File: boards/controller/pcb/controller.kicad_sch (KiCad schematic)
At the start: 5 parts, among them J101 Battery, J102 Load Switch 5V, J103 Load Switch 15 V isolated

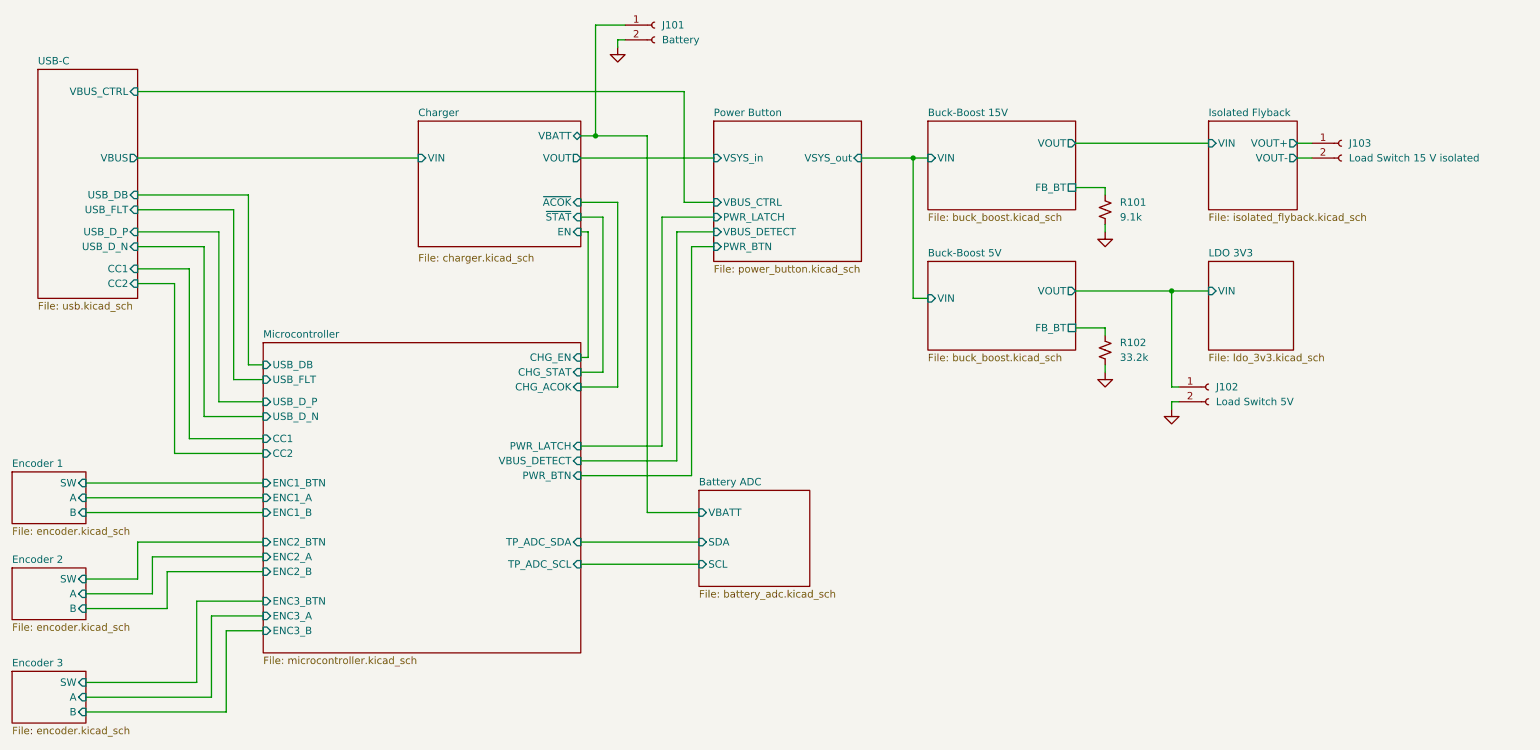
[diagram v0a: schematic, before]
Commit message: controller: pcb: Update schematic
Signed-off-by: Nicholas Loehrke <nicholasnloehrke@gmail.com>
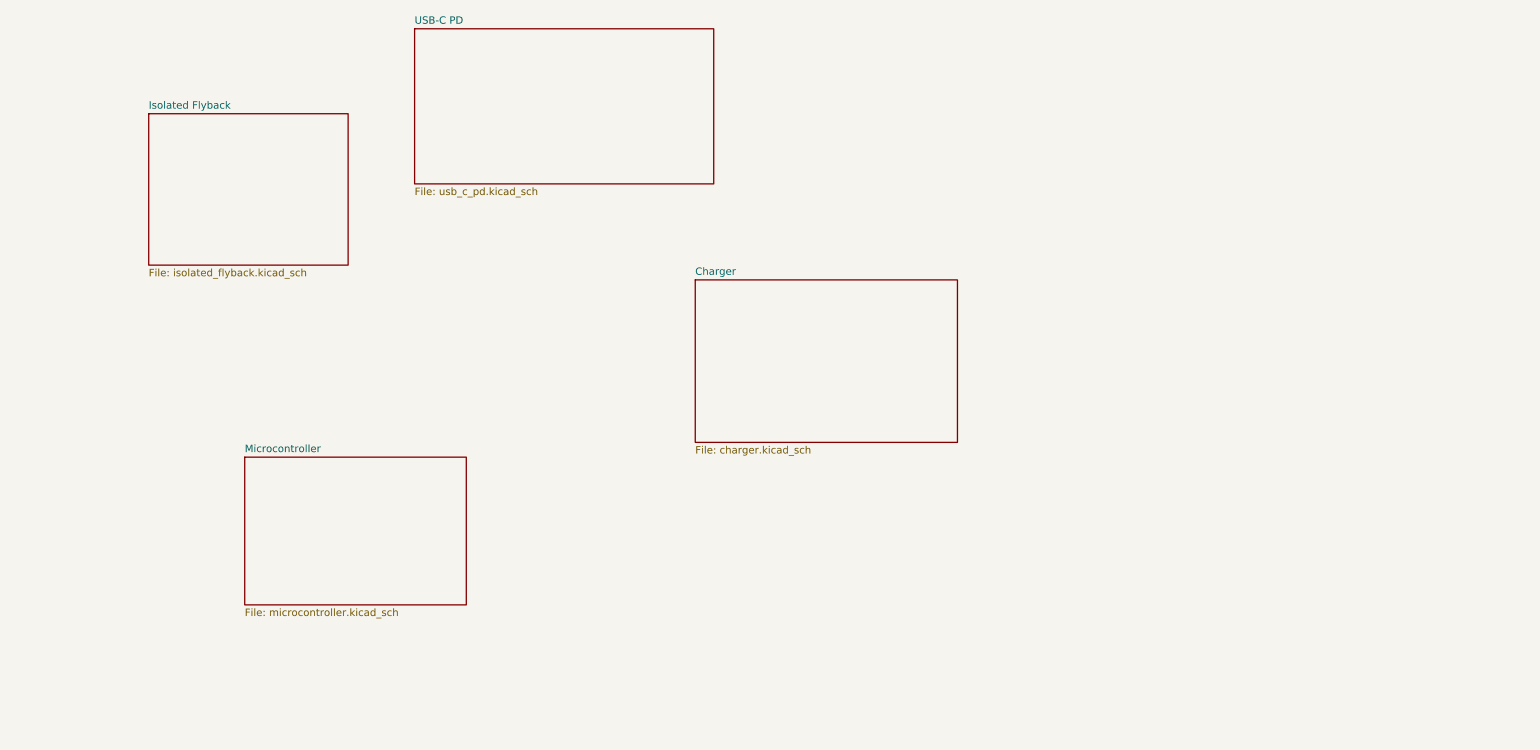
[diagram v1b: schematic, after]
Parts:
- removed J101: Battery, symbol Connector:Conn_01x02_Socket
- removed J102: Load Switch 5V, symbol Connector:Conn_01x02_Socket
- removed J103: Load Switch 15 V isolated, symbol Connector:Conn_01x02_Socket
- removed R101: 9.1k, symbol Device:R_Small_US
- removed R102: 33.2k, symbol Device:R_Small_US
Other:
- removed sheet Battery ADC
- removed sheet Buck-Boost 15V
- removed sheet Buck-Boost 5V
- removed sheet Encoder 1
- removed sheet Encoder 2
- removed sheet Encoder 3
- removed sheet LDO 3V3
- removed sheet Power Button
- removed sheet USB-C
- added sheet USB-C PD (usb_c_pd.kicad_sch)
- sheet Charger ports: added none; removed EN, VBATT, VIN, VOUT, ~{ACOK}, ~{STAT}
- sheet Isolated Flyback ports: added none; removed VIN, VOUT+, VOUT-
- sheet Microcontroller ports: added none; removed CC1, CC2, CHG_ACOK, CHG_EN, CHG_STAT, ENC1_A, ENC1_B, ENC1_BTN, ENC2_A, ENC2_B, ENC2_BTN, ENC3_A, ENC3_B, ENC3_BTN, PWR_BTN, PWR_LATCH, TP_ADC_SCL, TP_ADC_SDA, USB_DB, USB_D_N, USB_D_P, USB_FLT, VBUS_DETECT

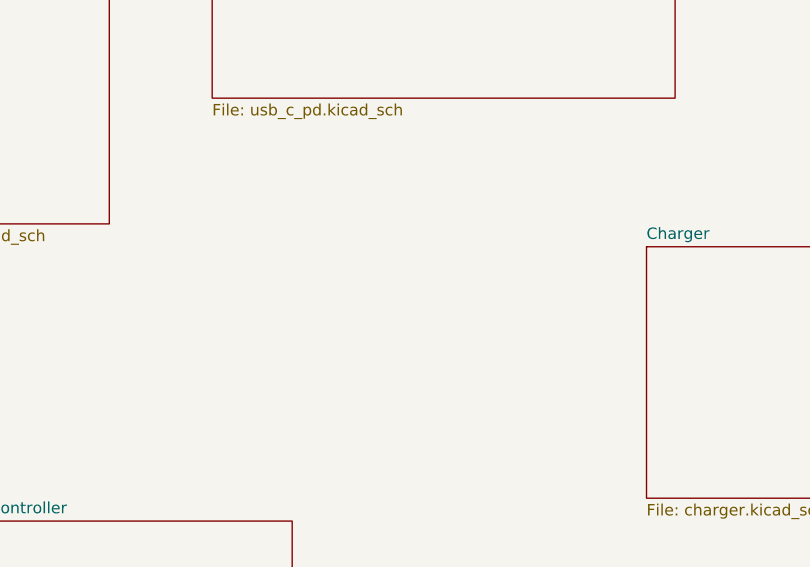
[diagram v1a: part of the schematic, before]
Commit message: controller: pcb: Update schematic
Signed-off-by: Nicholas Loehrke <nicholasnloehrke@gmail.com>
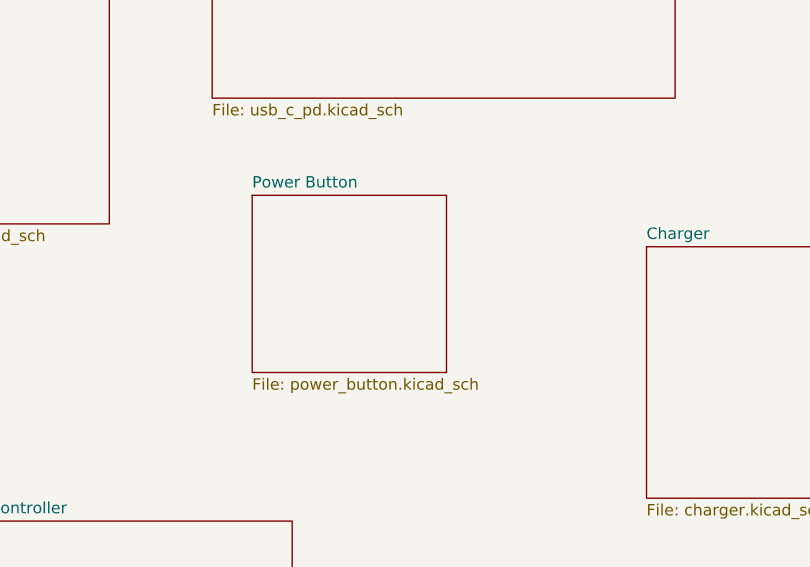
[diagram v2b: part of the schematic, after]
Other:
- added sheet Power Button (power_button.kicad_sch)
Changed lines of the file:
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@@
+		)
+	)
+	(sheet
+		(at 99.06 78.74)
+		(size 21.59 19.685)
+		(exclude_from_sim no)
+		(in_bom yes)
+		(on_board yes)
+		(dnp no)
+		(fields_autoplaced yes)
+		(stroke
+			(width 0.1524)
+			(type solid)
+		)
+		(fill
+			(color 0 0 0 0.0000)
+		)
+		(property "Sheetname" "Power Button"
+			(at 99.06 78.0284 0)
+			(effects
+				(font
+					(size 1.27 1.27)
+				)
+				(justify left bottom)
+			)
+		)
+		(property "Sheetfile" "power_button.kicad_sch"
+			(at 99.06 99.0096 0)
+			(effects
+				(font
+					(size 1.27 1.27)
+				)
+				(justify left top)
+			)
+		)
+		(instances
+			(project "controller"
+				(path "/5caba13a-97ae-46d4-856f-900b12012fd8"
+					(page "6")
+				)
+			)
 		)
 	)

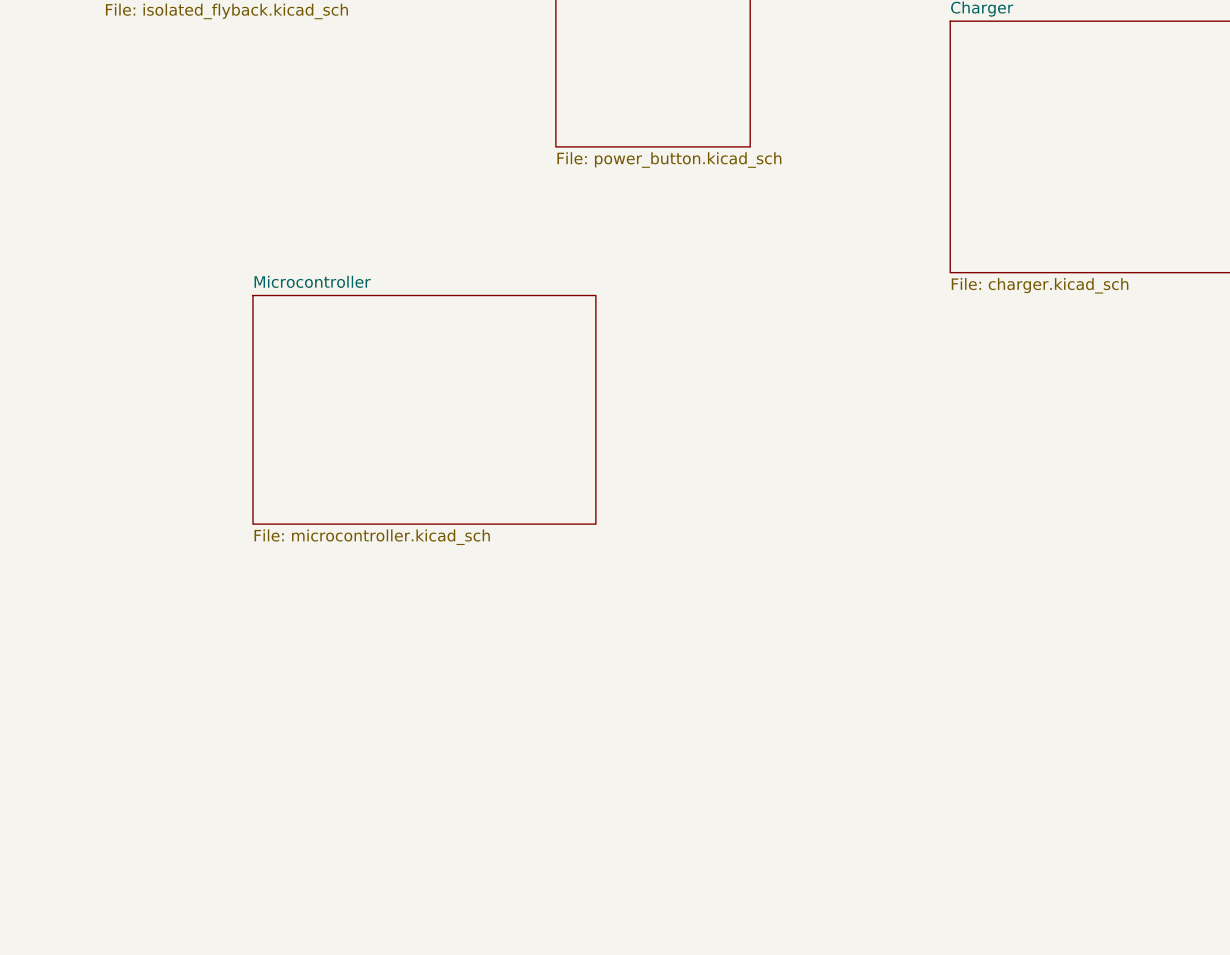
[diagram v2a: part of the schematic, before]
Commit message: controller: pcb: Update schematic
Signed-off-by: Nicholas Loehrke <nicholasnloehrke@gmail.com>
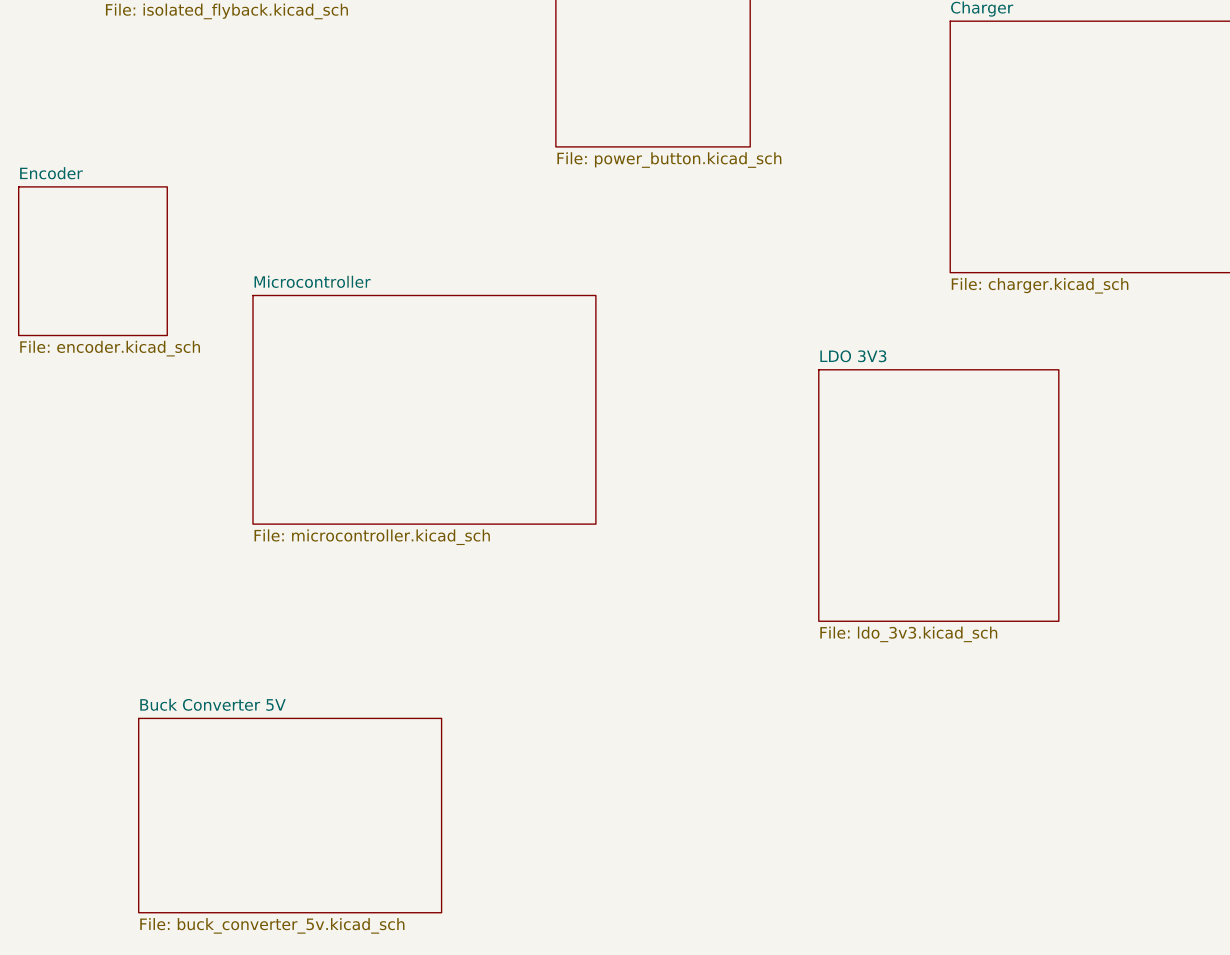
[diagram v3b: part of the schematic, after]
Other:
- added sheet Buck Converter 5V (buck_converter_5v.kicad_sch)
- added sheet Encoder (encoder.kicad_sch)
- added sheet LDO 3V3 (ldo_3v3.kicad_sch)
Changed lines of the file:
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@@
 	(paper "A4")
+	(sheet
+		(at 128.27 123.19)
+		(size 26.67 27.94)
+		(exclude_from_sim no)
+		(in_bom yes)
+		(on_board yes)
+		(dnp no)
+		(fields_autoplaced yes)
+		(stroke
+			(width 0.1524)
+			(type solid)
+		)
+		(fill
+			(color 0 0 0 0.0000)
+		)
+		(property "Sheetname" "LDO 3V3"
+			(at 128.27 122.4784 0)
+			(effects
+				(font
+					(size 1.27 1.27)
+				)
+				(justify left bottom)
+			)
+		)
+		(property "Sheetfile" "ldo_3v3.kicad_sch"
+			(at 128.27 151.7146 0)
+			(effects
+				(font
+					(size 1.27 1.27)
+				)
+				(justify left top)
+			)
+		)
+		(instances
+			(project "controller"
+				(path "/5caba13a-97ae-46d4-856f-900b12012fd8"
+					(page "9")
+				)
+			)
+		)
+	)
 	(sheet
 		(at 94.615 41.275)
@@
 	)
 	(sheet
+		(at 39.37 102.87)
+		(size 16.51 16.51)
+		(exclude_from_sim no)
+		(in_bom yes)
+		(on_board yes)
+		(dnp no)
+		(fields_autoplaced yes)
+		(stroke
+			(width 0.1524)
+			(type solid)
+		)
+		(fill
+			(color 0 0 0 0.0000)
+		)
+		(property "Sheetname" "Encoder"
+			(at 39.37 102.1584 0)
+			(effects
+				(font
+					(size 1.27 1.27)
+				)
+				(justify left bottom)
+			)
+		)
+		(property "Sheetfile" "encoder.kicad_sch"
+			(at 39.37 119.9646 0)
+			(effects
+				(font
+					(size 1.27 1.27)
+				)
+				(justify left top)
+			)
+		)
+		(instances
+			(project "controller"
+				(path "/5caba13a-97ae-46d4-856f-900b12012fd8"
+					(page "7")
+				)
+			)
+		)
+	)
+	(sheet
 		(at 142.875 84.455)
 		(size 45.085 27.94)
@@
 				)
 			)
+		)
+	)
+	(sheet
+		(at 52.705 161.925)
+		(size 33.655 21.59)
+		(exclude_from_sim no)
+		(in_bom yes)
+		(on_board yes)
+		(dnp no)
+		(fields_autoplaced yes)
+		(stroke
+			(width 0.1524)
+			(type solid)
+		)
+		(fill
+			(color 0 0 0 0.0000)
+		)
+		(property "Sheetname" "Buck Converter 5V"
+			(at 52.705 161.2134 0)
+			(effects
+				(font
+					(size 1.27 1.27)
+				)
+				(justify left bottom)
+			)
+		)
+		(property "Sheetfile" "buck_converter_5v.kicad_sch"
+			(at 52.705 184.0996 0)
+			(effects
+				(font
+					(size 1.27 1.27)
+				)
+				(justify left top)
+			)
+		)
+		(instances
+			(project "controller"
+				(path "/5caba13a-97ae-46d4-856f-900b12012fd8"
+					(page "8")
+				)
+			)

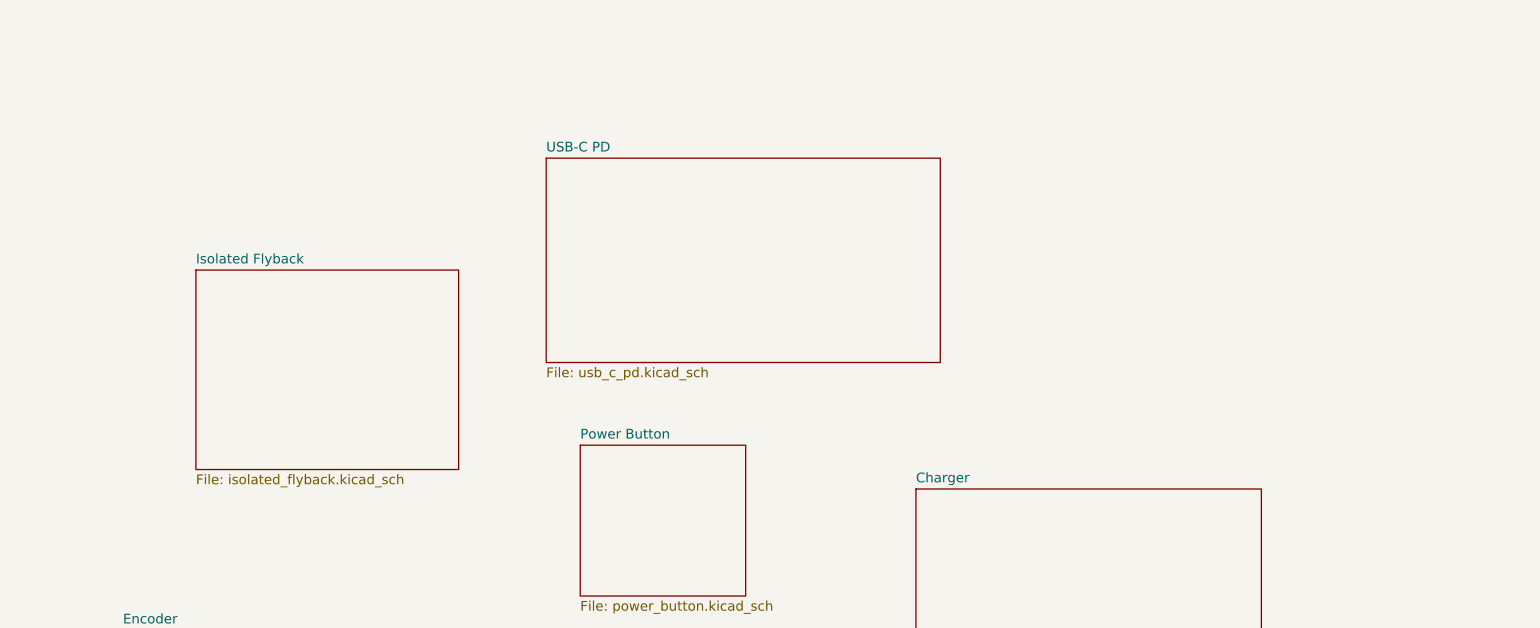
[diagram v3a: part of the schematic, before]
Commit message: controller: pcb: Update schematic
Signed-off-by: Nicholas Loehrke <nicholasnloehrke@gmail.com>
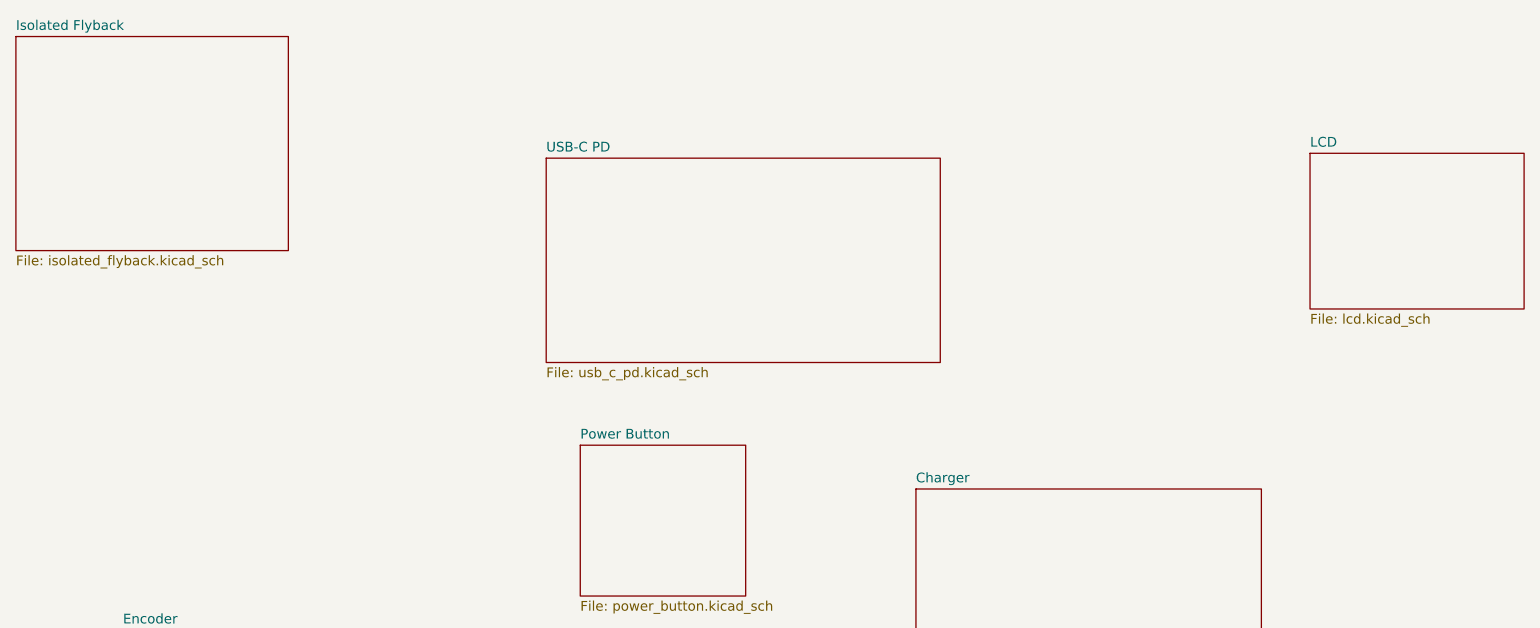
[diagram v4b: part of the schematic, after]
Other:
- added sheet LCD (lcd.kicad_sch)
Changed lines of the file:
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@@
 	)
 	(sheet
-		(at 48.895 55.88)
-		(size 34.29 26.035)
+		(at 194.31 40.64)
+		(size 27.94 20.32)
+		(exclude_from_sim no)
+		(in_bom yes)
+		(on_board yes)
+		(dnp no)
+		(fields_autoplaced yes)
+		(stroke
+			(width 0.1524)
+			(type solid)
+		)
+		(fill
+			(color 0 0 0 0.0000)
+		)
+		(property "Sheetname" "LCD"
+			(at 194.31 39.9284 0)
+			(effects
+				(font
+					(size 1.27 1.27)
+				)
+				(justify left bottom)
+			)
+		)
+		(property "Sheetfile" "lcd.kicad_sch"
+			(at 194.31 61.5446 0)
+			(effects
+				(font
+					(size 1.27 1.27)
+				)
+				(justify left top)
+			)
+		)
+		(instances
+			(project "controller"
+				(path "/5caba13a-97ae-46d4-856f-900b12012fd8"
+					(page "10")
+				)
+			)
+		)
+	)
+	(sheet
+		(at 25.4 25.4)
+		(size 35.56 27.94)
 		(exclude_from_sim no)
 		(in_bom yes)
@@
 		)
 		(property "Sheetname" "Isolated Flyback"
-			(at 48.895 55.1684 0)
+			(at 25.4 24.6884 0)
 			(effects
 				(font
@@
 		)
 		(property "Sheetfile" "isolated_flyback.kicad_sch"
-			(at 48.895 82.4996 0)
+			(at 25.4 53.9246 0)
 			(effects
 				(font
